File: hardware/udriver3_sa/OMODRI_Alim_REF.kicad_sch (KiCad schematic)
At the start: 3 parts, among them U15 LT6654AIS6-3

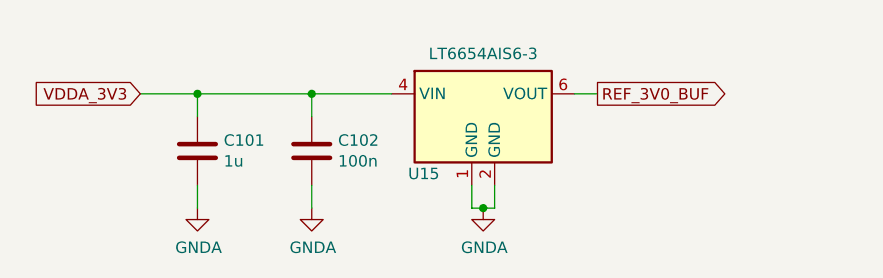
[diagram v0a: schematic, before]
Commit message: Third release of uOmodri Single Axis (uOmodri_SA). Add Test points.
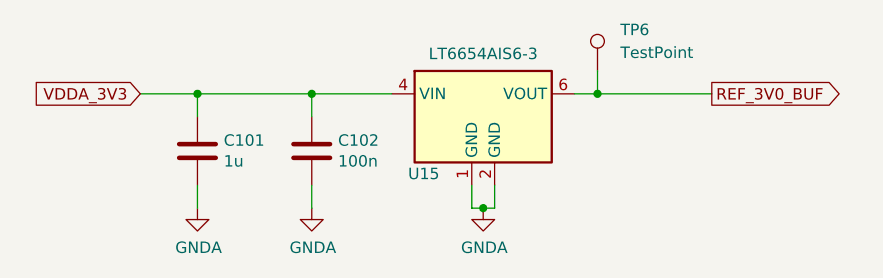
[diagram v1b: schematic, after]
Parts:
- added TP6: TestPoint, TestPoint:TestPoint_Pad_D1.0mm, symbol Connector:TestPoint
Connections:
- net REF_3V0_BUF: now also TP6.1
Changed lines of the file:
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@@
 		(color 0 0 0 0)
 	)
+	(junction
+		(at 165.1 76.2)
+		(diameter 0)
+		(color 0 0 0 0)
+	)
 	(wire
 		(pts
@@
 	(wire
 		(pts
+			(xy 165.1 76.2) (xy 177.8 76.2)
+		)
+		(stroke
+			(width 0)
+			(type default)
+		)
+	)
+	(wire
+		(pts
 			(xy 120.65 76.2) (xy 120.65 78.74)
 		)
@@
 		(pts
 			(xy 133.35 76.2) (xy 142.24 76.2)
+		)
+		(stroke
+			(width 0)
+			(type default)
+		)
+	)
+	(wire
+		(pts
+			(xy 165.1 73.66) (xy 165.1 76.2)
 		)
 		(stroke
@@
 	(global_label "REF_3V0_BUF"
 		(shape output)
-		(at 165.1 76.2 0)
+		(at 177.8 76.2 0)
 		(fields_autoplaced yes)
 		(effects
@@
 		)
 		(property "Intersheetrefs" "${INTERSHEET_REFS}"
-			(at 165.1 76.2 0)
+			(at 177.8 76.2 0)
 			(effects
 				(font
@@
 		)
 		(property "Références Inter-Feuilles" "${INTERSHEET_REFS}"
-			(at -15.875 -4.445 0)
+			(at -3.175 -4.445 0)
 			(effects
 				(font
@@
 					(unit 1)
 				)
+			)
+		)
+	)
+	(symbol
+		(lib_id "Connector:TestPoint")
+		(at 165.1 73.66 0)
+		(unit 1)
+		(exclude_from_sim no)
+		(in_bom no)
+		(on_board yes)
+		(dnp no)
+		(fields_autoplaced yes)
+		(property "Reference" "TP6"
+			(at 167.64 69.0879 0)
+			(effects
+				(font
+					(size 1.27 1.27)
+				)
+				(justify left)
+			)
+		)
+		(property "Value" "TestPoint"
+			(at 167.64 71.6279 0)
+			(effects
+				(font
+					(size 1.27 1.27)
+				)
+				(justify left)
+			)
+		)
+		(property "Footprint" "TestPoint:TestPoint_Pad_D1.0mm"
+			(at 170.18 73.66 0)
+			(effects
+				(font
+					(size 1.27 1.27)
+				)
+				(hide yes)
+			)
+		)
+		(property "Datasheet" "~"
+			(at 170.18 73.66 0)
+			(effects
+				(font
+					(size 1.27 1.27)
+				)
+				(hide yes)
+			)
+		)
+		(property "Description" "test point"
+			(at 165.1 73.66 0)
+			(effects
+				(font
+					(size 1.27 1.27)
+				)
+				(hide yes)
+			)
+		)
+		(pin "1"
+		)
+		(instances
+			(project "omodri_sa_laas"
+				(path "/de5b13f0-933a-4c4d-9979-13dc57b13241/00000000-0000-0000-0000-00005f3a3f16/00000000-0000-0000-0000-00005f5c0183"
+					(reference "TP6")
+					(unit 1)
+				)

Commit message: Update on uOmodri_SA. Remove USB, com SPI & debug connectors for integration into Myactuator motors. Connectors replaced by a ZIF connector.
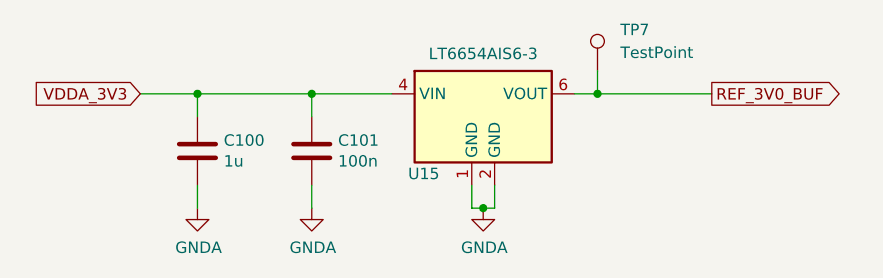
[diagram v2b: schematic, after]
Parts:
- renumbered C101 to C100, C102 to C101, TP6 to TP7
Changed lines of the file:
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@@
 	(title_block
 		(title "Open MOtor DRiver Initiative  - Single Axis (OMODRI_SA)")
-		(date "2024-03-20")
+		(date "2024-11-08")
 		(rev "1.0")
 		(company "LAAS/CNRS")
@@
 		(on_board yes)
 		(dnp no)
-		(property "Reference" "#PWR0163"
+		(property "Reference" "#PWR0148"
 			(at 120.65 95.25 0)
 			(effects
@@
 			(project "omodri_sa_laas"
 				(path "/de5b13f0-933a-4c4d-9979-13dc57b13241/00000000-0000-0000-0000-00005f3a3f16/00000000-0000-0000-0000-00005f5c0183"
-					(reference "#PWR0163")
+					(reference "#PWR0148")
 					(unit 1)
 				)
@@
 		(on_board yes)
 		(dnp no)
-		(property "Reference" "#PWR0164"
+		(property "Reference" "#PWR0149"
 			(at 133.35 95.25 0)
 			(effects
@@
 			(project "omodri_sa_laas"
 				(path "/de5b13f0-933a-4c4d-9979-13dc57b13241/00000000-0000-0000-0000-00005f3a3f16/00000000-0000-0000-0000-00005f5c0183"
-					(reference "#PWR0164")
+					(reference "#PWR0149")
 					(unit 1)
 				)
@@
 		(on_board yes)
 		(dnp no)
-		(property "Reference" "#PWR0165"
+		(property "Reference" "#PWR0150"
 			(at 152.4 95.25 0)
 			(effects
@@
 			(project "omodri_sa_laas"
 				(path "/de5b13f0-933a-4c4d-9979-13dc57b13241/00000000-0000-0000-0000-00005f3a3f16/00000000-0000-0000-0000-00005f5c0183"
-					(reference "#PWR0165")
+					(reference "#PWR0150")
 					(unit 1)
 				)
@@
 		(on_board yes)
 		(dnp no)
-		(property "Reference" "C102"
+		(property "Reference" "C101"
 			(at 136.271 81.3816 0)
 			(effects
@@
 			(project "omodri_sa_laas"
 				(path "/de5b13f0-933a-4c4d-9979-13dc57b13241/00000000-0000-0000-0000-00005f3a3f16/00000000-0000-0000-0000-00005f5c0183"
-					(reference "C102")
+					(reference "C101")
 					(unit 1)
 				)
@@
 		(on_board yes)
 		(dnp no)
-		(property "Reference" "C101"
+		(property "Reference" "C100"
 			(at 123.571 81.3816 0)
 			(effects
@@
 			(project "omodri_sa_laas"
 				(path "/de5b13f0-933a-4c4d-9979-13dc57b13241/00000000-0000-0000-0000-00005f3a3f16/00000000-0000-0000-0000-00005f5c0183"
-					(reference "C101")
+					(reference "C100")
 					(unit 1)
 				)
@@
 		(dnp no)
 		(fields_autoplaced yes)
-		(property "Reference" "TP6"
+		(property "Reference" "TP7"
 			(at 167.64 69.0879 0)
 			(effects
@@
 			(project "omodri_sa_laas"
 				(path "/de5b13f0-933a-4c4d-9979-13dc57b13241/00000000-0000-0000-0000-00005f3a3f16/00000000-0000-0000-0000-00005f5c0183"
-					(reference "TP6")
+					(reference "TP7")
 					(unit 1)
 				)
